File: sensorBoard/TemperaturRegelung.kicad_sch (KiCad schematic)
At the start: 17 parts, among them J2 Conn_01x02, Q1 NTD3055, Q3 2SC4213, U4 LM75C

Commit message: added the footprints, connectors left
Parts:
- C4: footprint (none) -> Capacitor_SMD:C_0805_2012Metric
- R1, R10, R11, R12, R2, R3, R4, R5, R7, R8, R9: footprint (none) -> Resistor_SMD:R_0805_2012Metric
- U13: footprint (none) -> Package_TO_SOT_SMD:SC-74-6_1.55x2.9mm_P0.95mm
- U4: footprint (none) -> Package_SO:TSSOP-8_3x3mm_P0.65mm
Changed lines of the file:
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@@
 			)
 		)
-		(property "Footprint" ""
+		(property "Footprint" "Resistor_SMD:R_0805_2012Metric"
 			(at 154.94 104.14 0)
 			(effects
@@
 			)
 		)
-		(property "Footprint" ""
+		(property "Footprint" "Resistor_SMD:R_0805_2012Metric"
 			(at 81.28 96.52 0)
 			(effects
@@
 			)
 		)
-		(property "Footprint" ""
+		(property "Footprint" "Package_SO:TSSOP-8_3x3mm_P0.65mm"
 			(at 98.806 88.9 0)
 			(effects
@@
 			)
 		)
-		(property "Datasheet" "http://www.ti.com/lit/ds/symlink/lm75b.pdf"
+		(property "Datasheet" "https://www.mouser.de/ProductDetail/NXP-Semiconductors/LM75ADP118?qs=LOCUfHb8d9vvCdlTDgESAg%3D%3D"
 			(at 84.582 79.375 0)
 			(effects
@@
 			)
 		)
-		(property "Footprint" ""
+		(property "Footprint" "Resistor_SMD:R_0805_2012Metric"
 			(at 55.88 96.52 0)
 			(effects
@@
 			)
 		)
-		(property "Footprint" ""
+		(property "Footprint" "Resistor_SMD:R_0805_2012Metric"
 			(at 68.58 96.52 0)
 			(effects
@@
 			)
 		)
-		(property "Footprint" ""
+		(property "Footprint" "Resistor_SMD:R_0805_2012Metric"
 			(at 171.45 104.14 0)
 			(effects
@@
 			)
 		)
-		(property "Footprint" ""
+		(property "Footprint" "Resistor_SMD:R_0805_2012Metric"
 			(at 55.88 80.01 0)
 			(effects
@@
 			)
 		)
-		(property "Footprint" ""
+		(property "Footprint" "Resistor_SMD:R_0805_2012Metric"
 			(at 68.58 80.01 0)
 			(effects
@@
 			)
 		)
-		(property "Footprint" ""
+		(property "Footprint" "Package_TO_SOT_SMD:SC-74-6_1.55x2.9mm_P0.95mm"
 			(at 161.29 36.83 0)
 			(effects
@@
 			)
 		)
-		(property "Footprint" ""
+		(property "Footprint" "Resistor_SMD:R_0805_2012Metric"
 			(at 128.27 104.14 0)
 			(effects
@@
 			)
 		)
-		(property "Footprint" ""
+		(property "Footprint" "Capacitor_SMD:C_0805_2012Metric"
 			(at 109.22 68.58 0)
 			(effects
@@
 			)
 		)
-		(property "Footprint" ""
+		(property "Footprint" "Resistor_SMD:R_0805_2012Metric"
 			(at 81.28 80.01 0)
 			(effects
@@
 			)
 		)
-		(property "Footprint" ""
+		(property "Footprint" "Resistor_SMD:R_0805_2012Metric"
 			(at 171.45 116.84 0)
 			(effects
@@
 			)
 		)
-		(property "Footprint" ""
+		(property "Footprint" "Resistor_SMD:R_0805_2012Metric"
 			(at 142.24 104.14 0)
 			(effects

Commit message: started the layout
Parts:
- J2: footprint (none) -> Connector_PinHeader_2.54mm:PinHeader_1x02_P2.54mm_Vertical
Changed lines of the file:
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@@
 			)
 		)
-		(property "Footprint" ""
+		(property "Footprint" "Connector_PinHeader_2.54mm:PinHeader_1x02_P2.54mm_Vertical"
 			(at 199.39 88.9 0)
 			(effects

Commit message: new two separate pcbs
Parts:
- removed R10, R12, R4, R8: 10k, Resistor_SMD:R_0805_2012Metric, symbol Device:R_Small
- removed R11, R7, R9: N.P., Resistor_SMD:R_0805_2012Metric, symbol Device:R_Small
- renumbered C4 to C29, J2 to J16, Q3 to Q11, Q1 to Q12, R3 to R53, R1 to R54, R2 to R55, R5 to R56, U4 to U21, U13 to U22
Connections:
- net GND: now also U21.5 (A2), U21.6 (A1), U21.7 (A0)

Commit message: Das erstes PCB ist fast fertig. Die Vias waren auf die Platine platziert und Poligon war gefüllt.
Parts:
- renumbered C29 to C46, J16 to J24, Q11 to Q19, Q12 to Q20, R53 to R41, R54 to R42, R55 to R43, R56 to R44, U21 to U33, U22 to U34
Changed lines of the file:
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@@
 		(dnp no)
 		(fields_autoplaced yes)
-		(property "Reference" "#PWR0137"
+		(property "Reference" "#PWR0219"
 			(at 101.6 66.04 0)
 			(effects
@@
 		(dnp no)
 		(fields_autoplaced yes)
-		(property "Reference" "R55"
+		(property "Reference" "R43"
 			(at 157.48 102.8699 0)
 			(effects
@@
 		(on_board yes)
 		(dnp no)
-		(property "Reference" "U21"
+		(property "Reference" "U33"
 			(at 102.87 82.296 0)
 			(effects
@@
 		(dnp no)
 		(fields_autoplaced yes)
-		(property "Reference" "#PWR0140"
+		(property "Reference" "#PWR0222"
 			(at 148.59 97.79 0)
 			(effects
@@
 		(dnp no)
 		(fields_autoplaced yes)
-		(property "Reference" "#PWR0139"
+		(property "Reference" "#PWR0221"
 			(at 109.22 78.74 0)
 			(effects
@@
 		(dnp no)
 		(fields_autoplaced yes)
-		(property "Reference" "#PWR0146"
+		(property "Reference" "#PWR0228"
 			(at 191.77 130.81 0)
 			(effects
@@
 		(dnp no)
 		(fields_autoplaced yes)
-		(property "Reference" "#PWR0132"
+		(property "Reference" "#PWR0214"
 			(at 55.88 107.95 0)
 			(effects
@@
 		(dnp no)
 		(fields_autoplaced yes)
-		(property "Reference" "#PWR0136"
+		(property "Reference" "#PWR0218"
 			(at 81.28 107.95 0)
 			(effects
@@
 		(dnp no)
 		(fields_autoplaced yes)
-		(property "Reference" "R56"
+		(property "Reference" "R44"
 			(at 173.99 102.8699 0)
 			(effects
@@
 		(dnp no)
 		(fields_autoplaced yes)
-		(property "Reference" "#PWR0143"
+		(property "Reference" "#PWR0225"
 			(at 161.29 62.23 0)
 			(effects
@@
 		(dnp no)
 		(fields_autoplaced yes)
-		(property "Reference" "#PWR0142"
+		(property "Reference" "#PWR0224"
 			(at 161.29 31.75 0)
 			(effects
@@
 		(dnp no)
 		(fields_autoplaced yes)
-		(property "Reference" "Q11"
+		(property "Reference" "Q19"
 			(at 157.48 115.5699 0)
 			(effects
@@
 		(dnp no)
 		(fields_autoplaced yes)
-		(property "Reference" "U22"
+		(property "Reference" "U34"
 			(at 163.4841 30.48 0)
 			(effects
@@
 		(dnp no)
 		(fields_autoplaced yes)
-		(property "Reference" "R53"
+		(property "Reference" "R41"
 			(at 130.81 102.8699 0)
 			(effects
@@
 		(dnp no)
 		(fields_autoplaced yes)
-		(property "Reference" "Q12"
+		(property "Reference" "Q20"
 			(at 195.58 107.9499 0)
 			(effects
@@
 		(dnp no)
 		(fields_autoplaced yes)
-		(property "Reference" "#PWR0145"
+		(property "Reference" "#PWR0227"
 			(at 191.77 88.9 0)
 			(effects
@@
 		(dnp no)
 		(fields_autoplaced yes)
-		(property "Reference" "C29"
+		(property "Reference" "C46"
 			(at 111.76 67.3162 0)
 			(effects
@@
 		(dnp no)
 		(fields_autoplaced yes)
-		(property "Reference" "#PWR0141"
+		(property "Reference" "#PWR0223"
 			(at 154.94 130.81 0)
 			(effects
@@
 		(dnp no)
 		(fields_autoplaced yes)
-		(property "Reference" "#PWR0134"
+		(property "Reference" "#PWR0216"
 			(at 68.58 107.95 0)
 			(effects
@@
 		(dnp no)
 		(fields_autoplaced yes)
-		(property "Reference" "#PWR0138"
+		(property "Reference" "#PWR0220"
 			(at 101.6 105.41 0)
 			(effects
@@
 		(dnp no)
 		(fields_autoplaced yes)
-		(property "Reference" "J16"
+		(property "Reference" "J24"
 			(at 201.93 88.8999 0)
 			(effects
@@
 		(dnp no)
 		(fields_autoplaced yes)
-		(property "Reference" "R54"
+		(property "Reference" "R42"
 			(at 144.78 102.8699 0)
 			(effects

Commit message: aktualisierte Platine mit verschiedenen Stecker
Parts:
- removed J24: Conn_01x02, Connector_PinHeader_2.54mm:PinHeader_1x02_P2.54mm_Vertical, symbol Connector_Generic:Conn_01x02
- added J4: Conn_01x04, 6432101004xx:643210100404, symbol Connector_Generic:Conn_01x04
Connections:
- net +12V: now also J4.1 (Pin_1), J4.4 (Pin_4)
- net at Q20.3 (D): now also J4.2 (Pin_2), J4.3 (Pin_3)
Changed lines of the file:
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@@
+	)
+	(junction
+		(at 198.12 91.44)
+		(diameter 0)
+		(color 0 0 0 0)
 	)
 	(junction
@@
 	)
 	(junction
+		(at 195.58 88.9)
+		(diameter 0)
+		(color 0 0 0 0)
+	)
+	(junction
 		(at 154.94 109.22)
 		(diameter 0)
@@
 	(wire
 		(pts
+			(xy 200.66 96.52) (xy 195.58 96.52)
+		)
+		(stroke
+			(width 0)
+			(type default)
+		)
+	)
+	(wire
+		(pts
 			(xy 128.27 116.84) (xy 142.24 116.84)
 		)
@@
 		)
 	)
+	(wire
+		(pts
+			(xy 195.58 88.9) (xy 195.58 96.52)
+		)
+		(stroke
+			(width 0)
+			(type default)
+		)
+	)
 	(polyline
 		(pts
@@
 	(wire
 		(pts
-			(xy 191.77 88.9) (xy 194.31 88.9)
+			(xy 191.77 88.9) (xy 195.58 88.9)
 		)
 		(stroke
@@
 	(wire
 		(pts
-			(xy 194.31 91.44) (xy 191.77 91.44)
+			(xy 191.77 91.44) (xy 198.12 91.44)
 		)
 		(stroke
@@
 	(wire
 		(pts
+			(xy 198.12 91.44) (xy 200.66 91.44)
+		)
+		(stroke
+			(width 0)
+			(type default)
+		)
+	)
+	(wire
+		(pts
 			(xy 91.44 91.44) (xy 81.28 91.44)
 		)
@@
 	(wire
 		(pts
+			(xy 195.58 88.9) (xy 200.66 88.9)
+		)
+		(stroke
+			(width 0)
+			(type default)
+		)
+	)
+	(wire
+		(pts
 			(xy 142.24 97.79) (xy 142.24 101.6)
 		)
@@
 	(wire
 		(pts
+			(xy 198.12 91.44) (xy 198.12 93.98)
+		)
+		(stroke
+			(width 0)
+			(type default)
+		)
+	)
+	(wire
+		(pts
 			(xy 191.77 85.09) (xy 191.77 88.9)
 		)
@@
 		(pts
 			(xy 137.16 19.05) (xy 180.34 19.05)
+		)
+		(stroke
+			(width 0)
+			(type default)
+		)
+	)
+	(wire
+		(pts
+			(xy 200.66 93.98) (xy 198.12 93.98)
 		)
 		(stroke
@@
 	)
 	(symbol
+		(lib_id "Connector_Generic:Conn_01x04")
+		(at 205.74 91.44 0)
+		(unit 1)
+		(exclude_from_sim no)
+		(in_bom yes)
+		(on_board yes)
+		(dnp no)
+		(fields_autoplaced yes)
+		(property "Reference" "J4"
+			(at 208.28 91.4399 0)
+			(effects
+				(font
+					(size 1.27 1.27)
+				)
+				(justify left)
+			)
+		)
+		(property "Value" "Conn_01x04"
+			(at 208.28 93.9799 0)
+			(effects
+				(font
+					(size 1.27 1.27)
+				)
+				(justify left)
+			)
+		)
+		(property "Footprint" "6432101004xx:643210100404"
+			(at 205.74 91.44 0)
+			(effects
+				(font
+					(size 1.27 1.27)
+				)
+				(hide yes)
+			)
+		)
+		(property "Datasheet" "~"
+			(at 205.74 91.44 0)
+			(effects
+				(font
+					(size 1.27 1.27)
+				)
+				(hide yes)
+			)
+		)
+		(property "Description" "Generic connector, single row, 01x04, script generated (kicad-library-utils/schlib/autogen/connector/)"
+			(at 205.74 91.44 0)
+			(effects
+				(font
+					(size 1.27 1.27)
+				)
+				(hide yes)
+			)
+		)
+		(pin "1"
+		)
+		(pin "4"
+		)
+		(pin "3"
+		)
+		(pin "2"
+		)
+		(instances
+			(project "sensorBoard"
+				(path "/df1584e9-54f0-49dc-b423-5f64048efa01/60fa4213-9bcb-42a7-994a-420953d9bcb7/daa9d051-a0c3-465e-98ed-e60c5b6e94ee"
+					(reference "J5")
+					(unit 1)
+				)
+				(path "/df1584e9-54f0-49dc-b423-5f64048efa01/99847452-c15f-478e-a49b-00c0f2bcd04b/7cd84f42-a581-49de-bb06-05a676a55f54"
+					(reference "J4")
+					(unit 1)
+				)
+			)
+		)
+	)
+	(symbol
 		(lib_id "power:GND")
 		(at 191.77 124.46 0)
@@
 					(unit 1)
 				)
-			)
-		)
-	)
-	(symbol
-		(lib_id "Connector_Generic:Conn_01x02")
-		(at 199.39 88.9 0)
-		(unit 1)
-		(exclude_from_sim no)
-		(in_bom yes)
-		(on_board yes)
-		(dnp no)
-		(fields_autoplaced yes)
-		(property "Reference" "J24"
-			(at 201.93 88.8999 0)
-			(effects
-				(font
-					(size 1.27 1.27)
-				)
-				(justify left)
-			)
-		)
-		(property "Value" "Conn_01x02"
-			(at 201.93 91.4399 0)
-			(effects
-				(font
-					(size 1.27 1.27)
-				)
-				(justify left)
-			)
-		)
-		(property "Footprint" "Connector_PinHeader_2.54mm:PinHeader_1x02_P2.54mm_Vertical"
-			(at 199.39 88.9 0)
-			(effects
-				(font
-					(size 1.27 1.27)
-				)
-				(hide yes)
-			)
-		)
-		(property "Datasheet" "~"
-			(at 199.39 88.9 0)
-			(effects
-				(font
-					(size 1.27 1.27)
-				)
-				(hide yes)
-			)
-		)
-		(property "Description" "Generic connector, single row, 01x02, script generated (kicad-library-utils/schlib/autogen/connector/)"
-			(at 199.39 88.9 0)
-			(effects
-				(font
-					(size 1.27 1.27)
-				)
-				(hide yes)
-			)
-		)
-		(pin "2"
-		)
-		(pin "1"
-		)
-		(instances
-			(project "sensorBoard"
-				(path "/df1584e9-54f0-49dc-b423-5f64048efa01/60fa4213-9bcb-42a7-994a-420953d9bcb7/daa9d051-a0c3-465e-98ed-e60c5b6e94ee"
-					(reference "J24")
-					(unit 1)
-				)
-				(path "/df1584e9-54f0-49dc-b423-5f64048efa01/99847452-c15f-478e-a49b-00c0f2bcd04b/7cd84f42-a581-49de-bb06-05a676a55f54"
-					(reference "J16")
-					(unit 1)
-				)

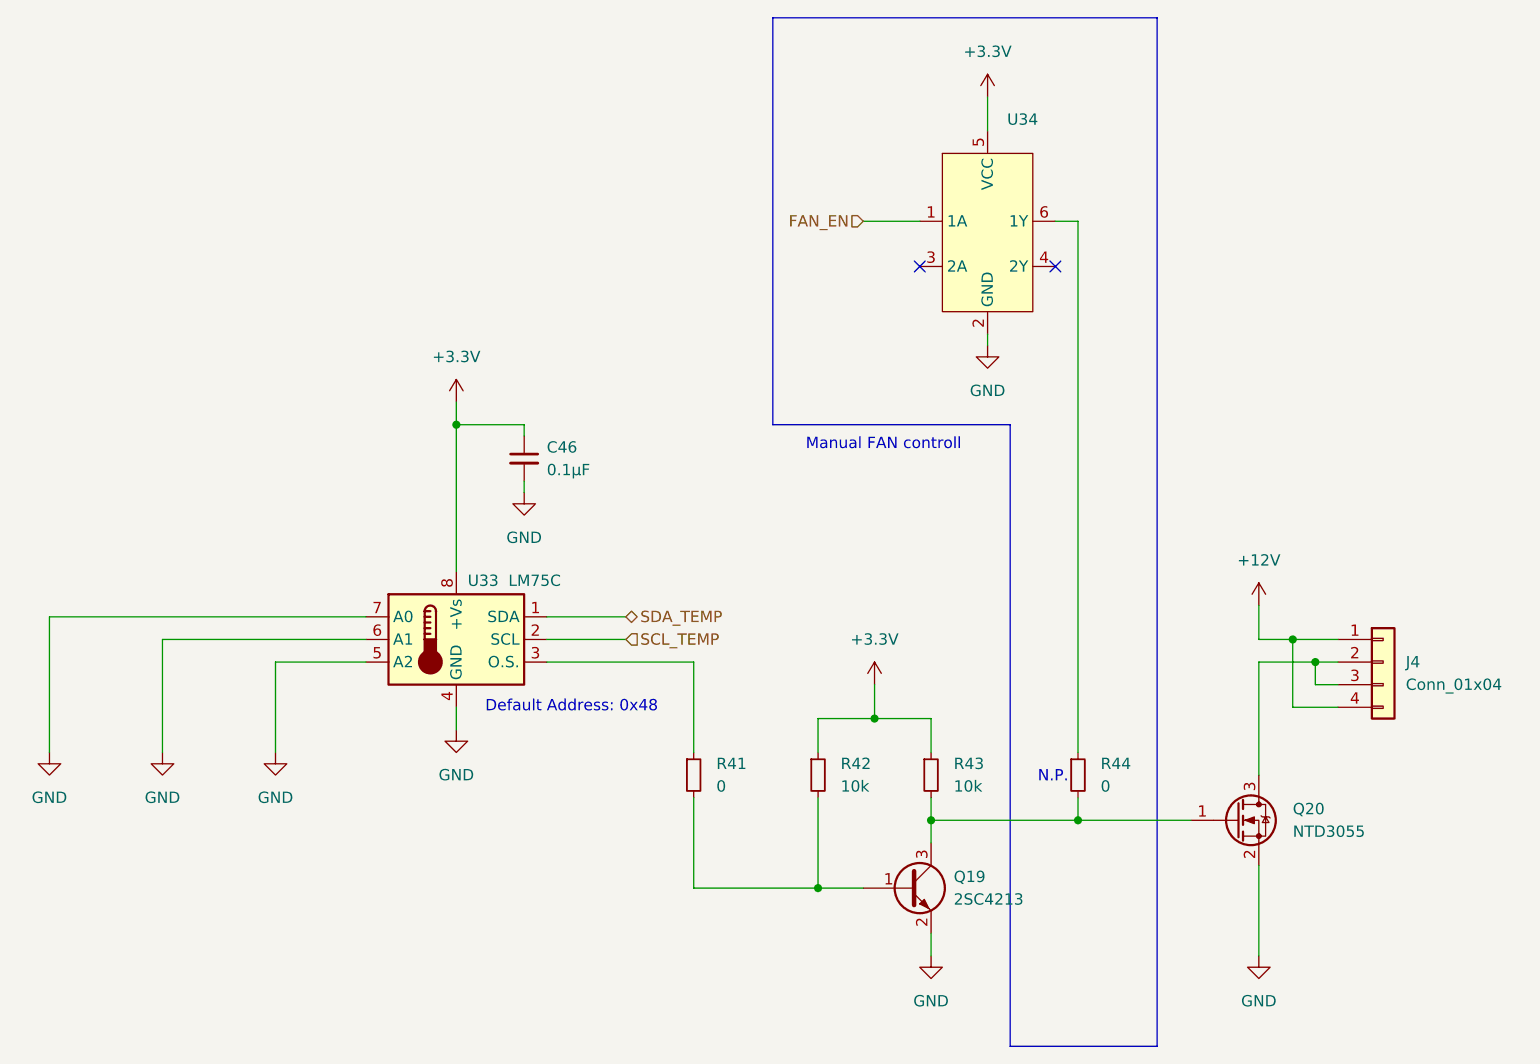
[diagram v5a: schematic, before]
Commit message: added old software + new PCB
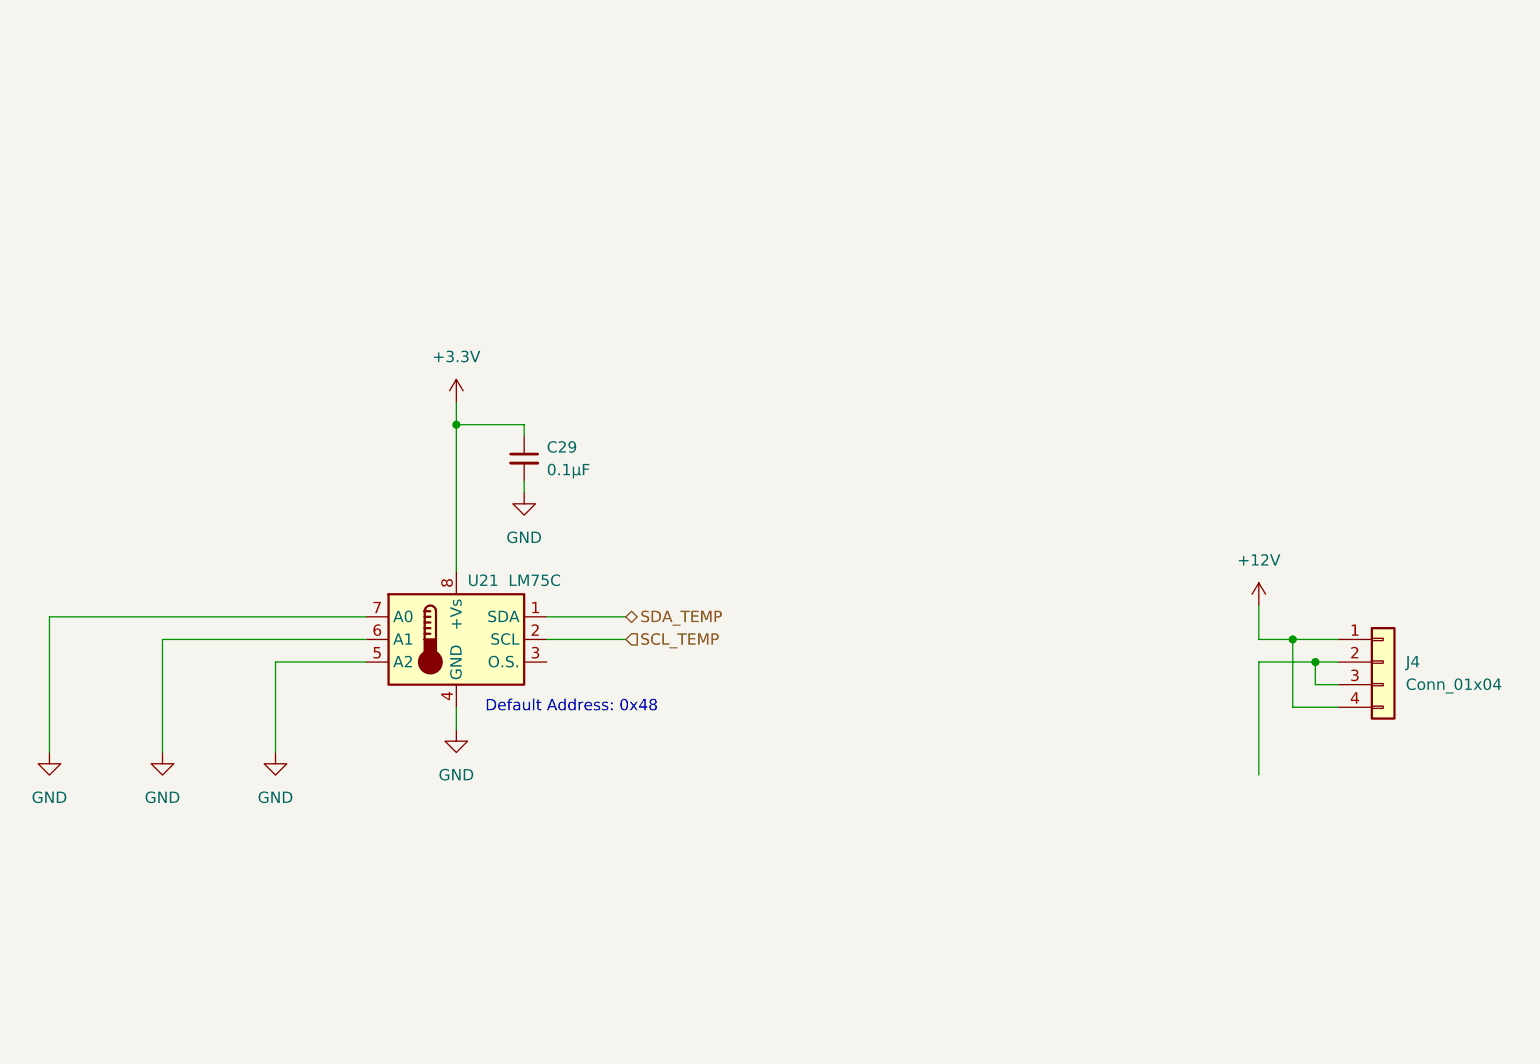
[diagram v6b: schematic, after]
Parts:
- removed Q19: 2SC4213, Package_TO_SOT_SMD:SOT-323_SC-70, symbol Transistor_BJT:2SC4213
- removed Q20: NTD3055, Package_TO_SOT_SMD:TO-252-2, symbol Transistor_FET:2N7002
- removed R41, R44: 0, Resistor_SMD:R_0805_2012Metric, symbol Device:R_Small
- removed R42, R43: 10k, Resistor_SMD:R_0805_2012Metric, symbol Device:R_Small
- removed U34: ~, Package_TO_SOT_SMD:SC-74-6_1.55x2.9mm_P0.95mm, symbol New_Library:SN74LVC2G34
- renumbered C46 to C29, U33 to U21
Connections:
- no-connect marks 2 -> 0
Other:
- note removed: "Manual FAN controll"
- note removed: "N.P."
